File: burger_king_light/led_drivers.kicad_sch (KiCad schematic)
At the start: 3 parts, among them IC2 IS32LT3178-GRLA3-TR, IC3 IS32LT3178-GRLA3-TR, IC4 IS32LT3178-GRLA3-TR

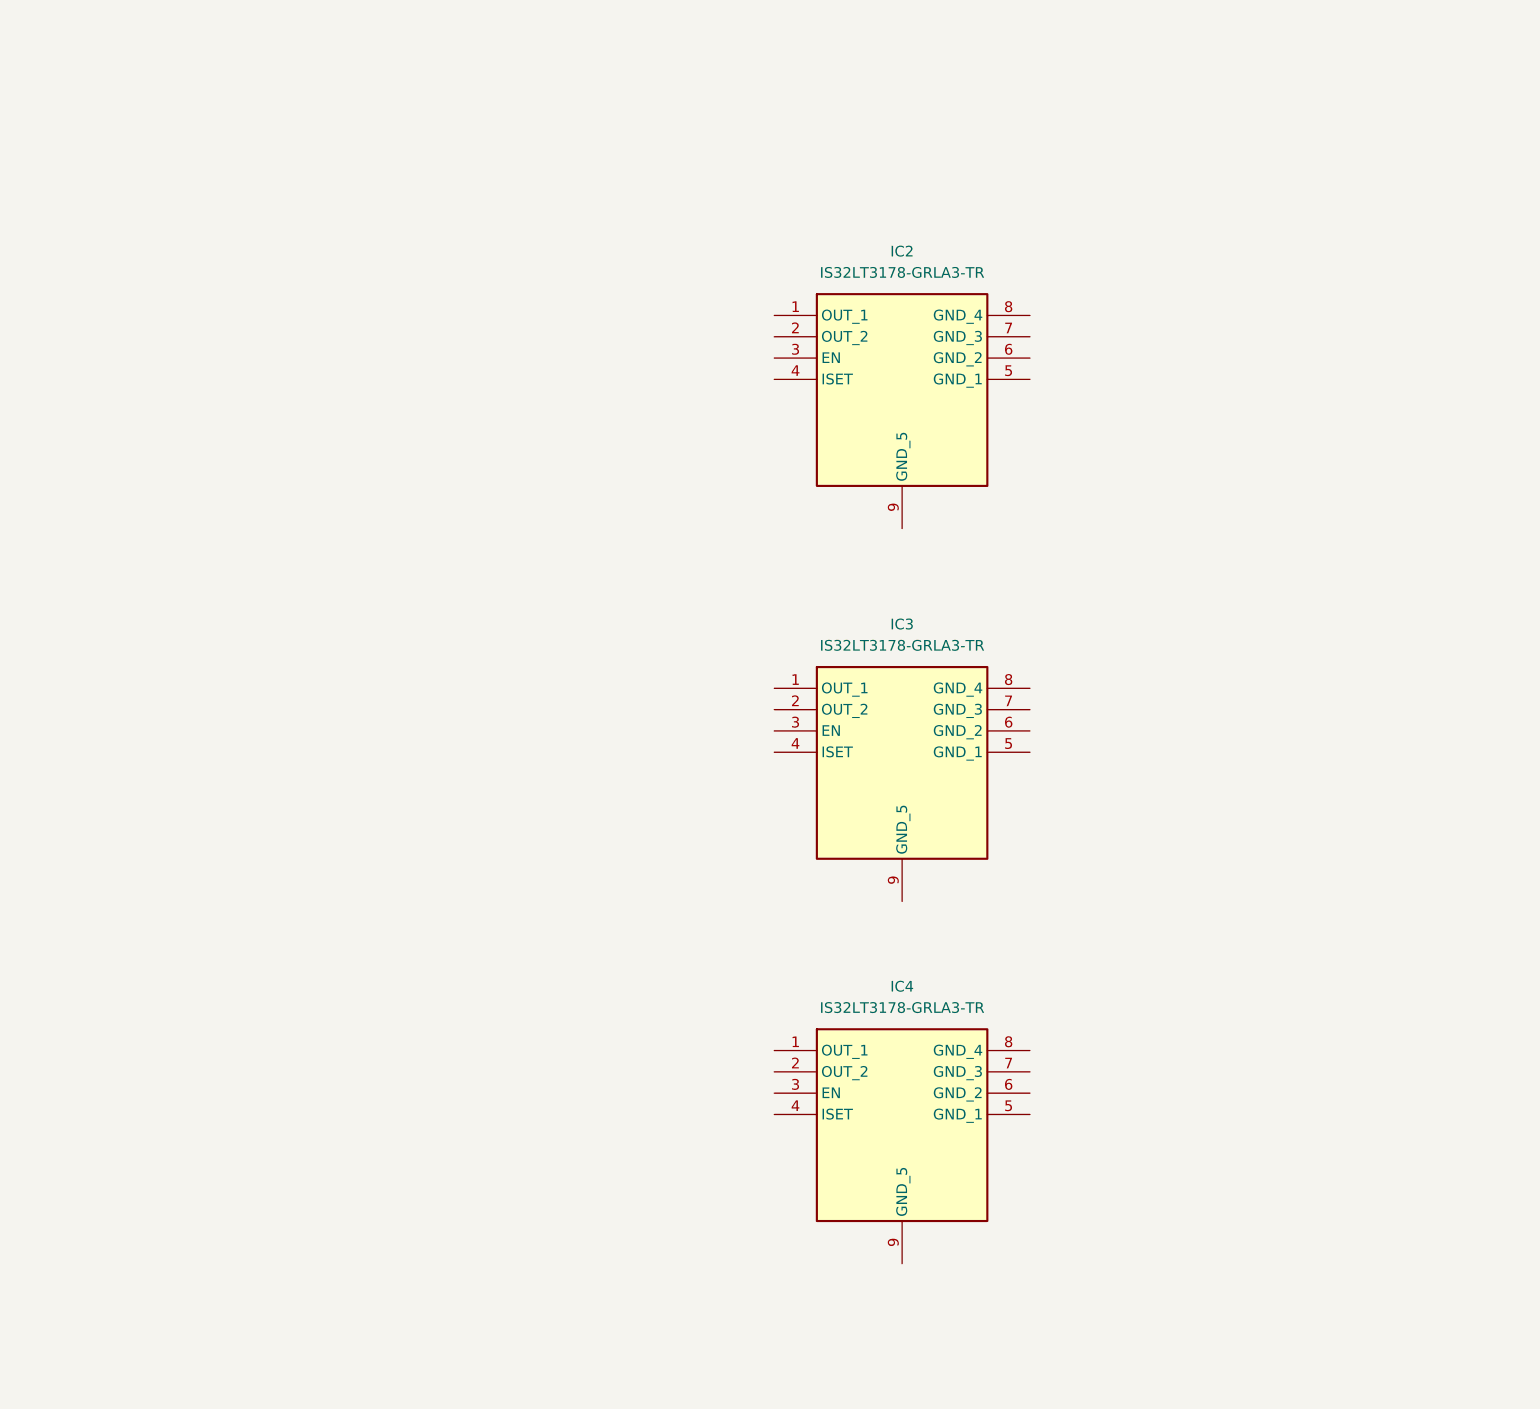
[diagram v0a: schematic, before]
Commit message: started wiring, designed Iset resistors
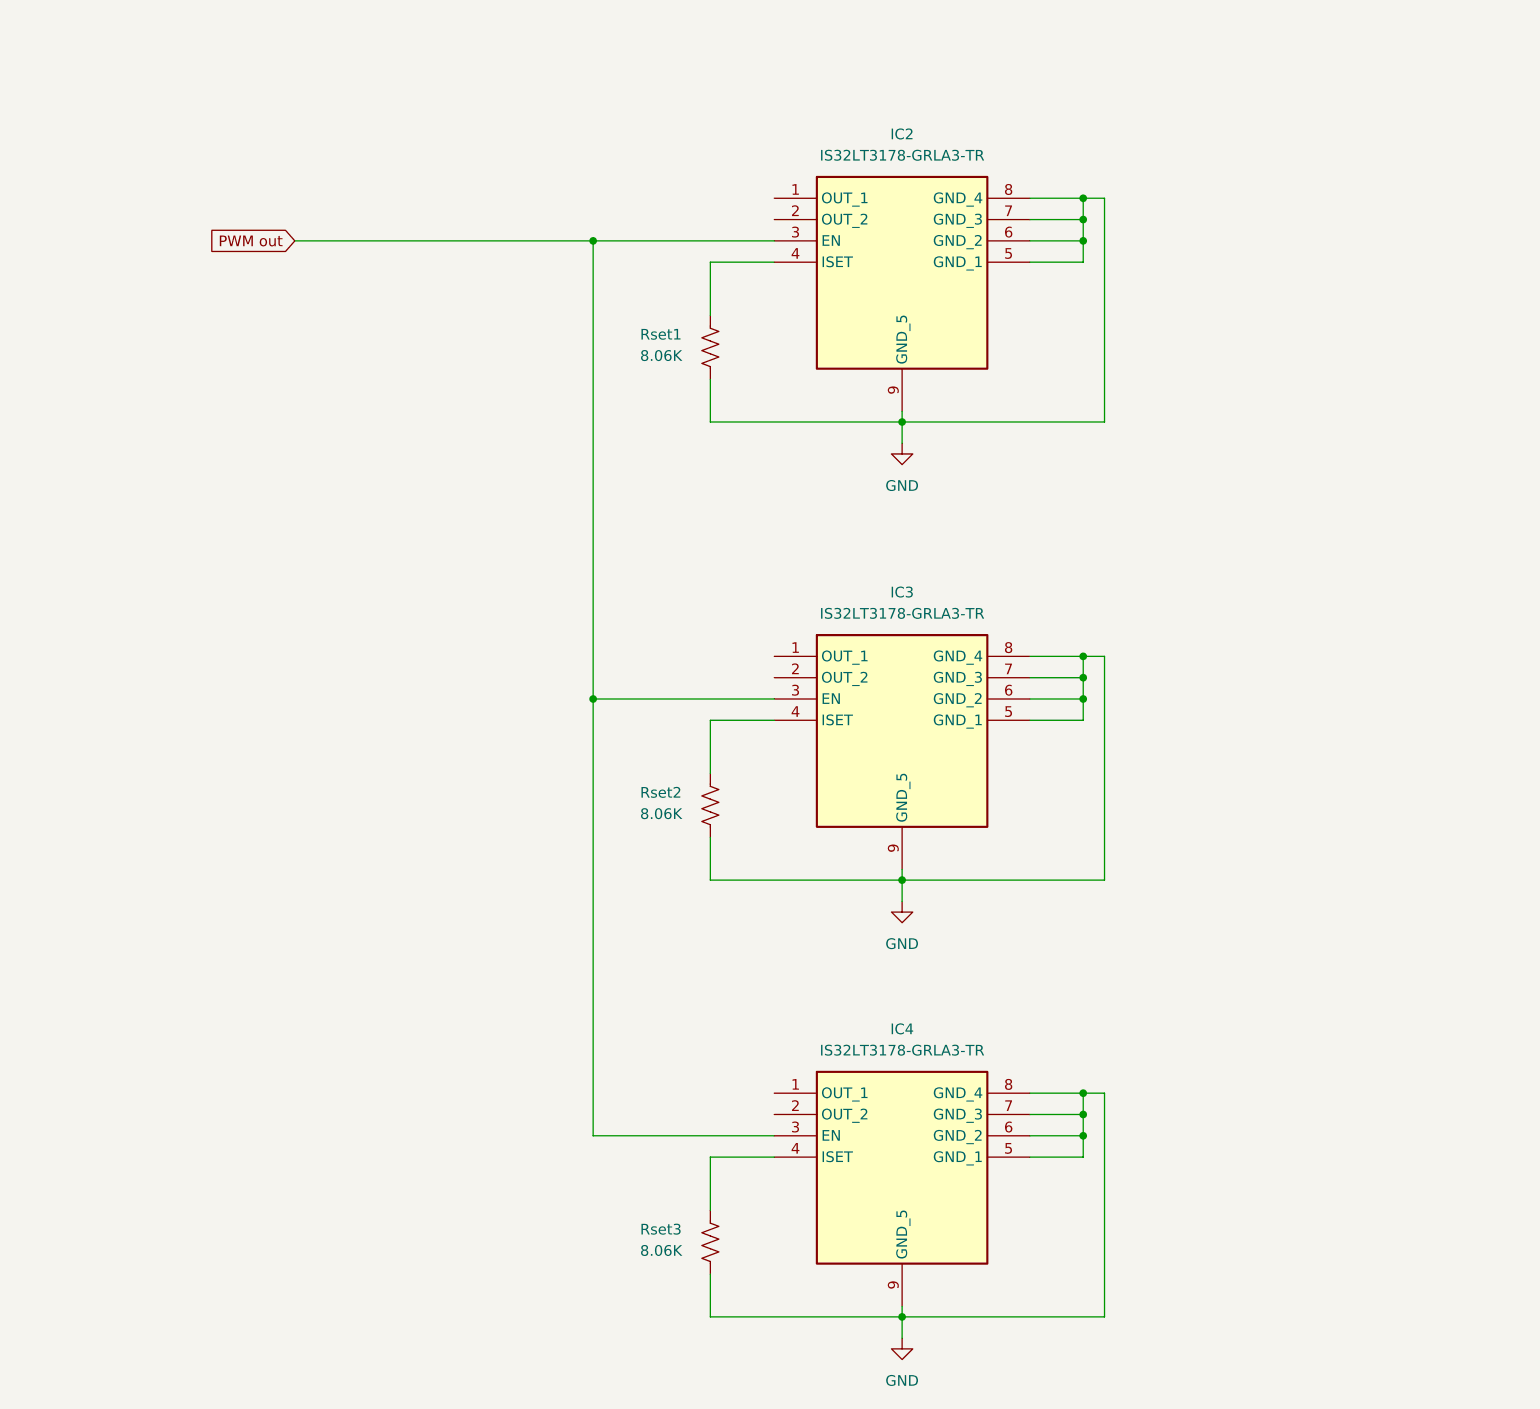
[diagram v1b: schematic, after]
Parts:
- added Rset1, Rset2, Rset3: 8.06K, Resistor_SMD:R_1206_3216Metric, symbol Device:R_US
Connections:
- net PWM out: now reaches IC2.3 (EN)
- net PWM out: now also IC3.3 (EN), IC4.3 (EN)
- net at IC2.4 (ISET): now also Rset1.1
- net GND: now reaches IC2.5 (GND_1)
- net GND: now also IC2.6 (GND_2), IC2.7 (GND_3), IC2.8 (GND_4), IC2.9 (GND_5), IC3.5 (GND_1), IC3.6 (GND_2), IC3.7 (GND_3), IC3.8 (GND_4), IC3.9 (GND_5), IC4.5 (GND_1), IC4.6 (GND_2), IC4.7 (GND_3), IC4.8 (GND_4), IC4.9 (GND_5), Rset1.2, Rset2.2, Rset3.2
- net at IC3.4 (ISET): now also Rset2.1
- net at IC4.4 (ISET): now also Rset3.1
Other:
- moved on the sheet: IC2, IC3, IC4

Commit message: finished layout
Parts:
- added Cled1, Cled2, Cled3: 100nF, Capacitor_SMD:C_0805_2012Metric, symbol Device:C
- added Cledout1, Cledout2, Cledout3: 1nF, Capacitor_SMD:C_0805_2012Metric, symbol Device:C
- added H1, H2, H3, H4, H5, H6: MountingHole_Pad, MountingHole:MountingHole_5.3mm_M5_DIN965_Pad_TopBottom, symbol Mechanical:MountingHole_Pad
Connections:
- net GND: now also Cled1.2, Cled2.2, Cled3.2, Cledout1.2, Cledout2.2, Cledout3.2
- net at IC2.1 (OUT_1): now also IC2.2 (OUT_2), Cledout1.1, H2.1
- net at IC3.1 (OUT_1): now also IC3.2 (OUT_2), Cledout2.1, H4.1
- net at IC4.1 (OUT_1): now also IC4.2 (OUT_2), Cledout3.1, H6.1
- new net +36V: Cled1.1, Cled2.1, Cled3.1, H1.1, H3.1, H5.1
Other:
- moved on the sheet: IC2, Rset1
